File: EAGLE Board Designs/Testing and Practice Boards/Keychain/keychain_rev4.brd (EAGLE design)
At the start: 27.9 x 27.9 mm, 14 parts, among them J1 USB4110, U1 LM555

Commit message: DRC and cam file
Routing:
- net GND: track 4.91 -> 2.53 mm
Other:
- board text added: "Hytech Racing 2024"
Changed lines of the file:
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@@
 <vertex x="19.05" y="6.35"/>
 </polygon>
+<text x="27.051" y="0.762" size="0.6858" layer="22" rot="MR0">Hytech Racing 2024</text>
 </plain>
 <attributes>
@@
 </class>
 </classes>
-<designrules name="default">
-<description language="de">&lt;b&gt;EAGLE Design Rules&lt;/b&gt;
-&lt;p&gt;
-Die Standard-Design-Rules sind so gewählt, dass sie für
-die meisten Anwendungen passen. Sollte ihre Platine
-besondere Anforderungen haben, treffen Sie die erforderlichen
-Einstellungen hier und speichern die Design Rules unter
-einem neuen Namen ab.</description>
-<description language="en">&lt;b&gt;EAGLE Design Rules&lt;/b&gt;
+<designrules name="JLCPCB (2 Layer)">
+<description language="en">&lt;b&gt;JLCPCB Design Rules (2 Layers)&lt;/b&gt;
 &lt;p&gt;
 The default Design Rules have been set to cover
-a wide range of applications. Your particular design
-may have different requirements, so please make the
-necessary adjustments and save your customized
-design rules under a new name.</description>
+a wide range of applications.
+&lt;p&gt;
+Source: &lt;a href=&quot;https://jlcpcb.com/capabilities/Capabilities&quot;&gt;JLCPCB&lt;/a&gt;
+&lt;/p&gt;</description>
 <param name="layerSetup" value="(1*16)"/>
 <param name="mtCopper" value="0.035mm 0.035mm 0.035mm 0.035mm 0.035mm 0.035mm 0.035mm 0.035mm 0.035mm 0.035mm 0.035mm 0.035mm 0.035mm 0.035mm 0.035mm 0.035mm"/>
-<param name="mtIsolate" value="1.5mm 0.15mm 0.2mm 0.15mm 0.2mm 0.15mm 0.2mm 0.15mm 0.2mm 0.15mm 0.2mm 0.15mm 0.2mm 0.15mm 0.2mm"/>
-<param name="mdWireWire" value="6mil"/>
-<param name="mdWirePad" value="6mil"/>
-<param name="mdWireVia" value="6mil"/>
-<param name="mdPadPad" value="6mil"/>
-<param name="mdPadVia" value="6mil"/>
-<param name="mdViaVia" value="6mil"/>
-<param name="mdSmdPad" value="6mil"/>
-<param name="mdSmdVia" value="6mil"/>
-<param name="mdSmdSmd" value="6mil"/>
+<param name="mtIsolate" value="1.53mm 0.15mm 0.2mm 0.15mm 0.2mm 0.15mm 0.2mm 0.15mm 0.2mm 0.15mm 0.2mm 0.15mm 0.2mm 0.15mm 0.2mm"/>
+<param name="mdWireWire" value="5mil"/>
+<param name="mdWirePad" value="5mil"/>
+<param name="mdWireVia" value="8mil"/>
+<param name="mdPadPad" value="5mil"/>
+<param name="mdPadVia" value="10mil"/>
+<param name="mdViaVia" value="20mil"/>
+<param name="mdSmdPad" value="5mil"/>
+<param name="mdSmdVia" value="10mil"/>
+<param name="mdSmdSmd" value="5mil"/>
 <param name="mdViaViaSameLayer" value="6mil"/>
 <param name="mnLayersViaInSmd" value="2"/>
-<param name="mdCopperDimension" value="40mil"/>
-<param name="mdDrill" value="6mil"/>
+<param name="mdCopperDimension" value="0.2mm"/>
+<param name="mdDrill" value="21mil"/>
 <param name="mdSmdStop" value="0mil"/>
-<param name="msWidth" value="6mil"/>
-<param name="msDrill" value="0.35mm"/>
+<param name="msWidth" value="5mil"/>
+<param name="msDrill" value="0.3mm"/>
 <param name="msMicroVia" value="9.99mm"/>
 <param name="msBlindViaRatio" value="0.5"/>
@@
 <param name="rvViaOuter" value="0.25"/>
 <param name="rvViaInner" value="0.25"/>
-<param name="rvMicroViaOuter" value="0.25"/>
-<param name="rvMicroViaInner" value="0.25"/>
-<param name="rlMinPadTop" value="10mil"/>
+<param name="rvMicroViaOuter" value="0"/>
+<param name="rvMicroViaInner" value="0"/>
+<param name="rlMinPadTop" value="6mil"/>
 <param name="rlMaxPadTop" value="20mil"/>
-<param name="rlMinPadInner" value="10mil"/>
+<param name="rlMinPadInner" value="6mil"/>
 <param name="rlMaxPadInner" value="20mil"/>
-<param name="rlMinPadBottom" value="10mil"/>
+<param name="rlMinPadBottom" value="6mil"/>
 <param name="rlMaxPadBottom" value="20mil"/>
-<param name="rlMinViaOuter" value="8mil"/>
-<param name="rlMaxViaOuter" value="20mil"/>
-<param name="rlMinViaInner" value="8mil"/>
-<param name="rlMaxViaInner" value="20mil"/>
-<param name="rlMinMicroViaOuter" value="4mil"/>
+<param name="rlMinViaOuter" value="6mil"/>
+<param name="rlMaxViaOuter" value="12mil"/>
+<param name="rlMinViaInner" value="6mil"/>
+<param name="rlMaxViaInner" value="12mil"/>
+<param name="rlMinMicroViaOuter" value="6mil"/>
 <param name="rlMaxMicroViaOuter" value="20mil"/>
-<param name="rlMinMicroViaInner" value="4mil"/>
+<param name="rlMinMicroViaInner" value="6mil"/>
 <param name="rlMaxMicroViaInner" value="20mil"/>
 <param name="psTop" value="-1"/>
 <param name="psBottom" value="-1"/>
-<param name="psFirst" value="-1"/>
+<param name="psFirst" value="0"/>
 <param name="psElongationLong" value="100"/>
 <param name="psElongationOffset" value="100"/>
 <param name="mvStopFrame" value="1"/>
 <param name="mvCreamFrame" value="0"/>
-<param name="mlMinStopFrame" value="4mil"/>
-<param name="mlMaxStopFrame" value="4mil"/>
+<param name="mlMinStopFrame" value="6mil"/>
+<param name="mlMaxStopFrame" value="6mil"/>
 <param name="mlMinCreamFrame" value="0mil"/>
 <param name="mlMaxCreamFrame" value="0mil"/>
-<param name="mlViaStopLimit" value="0mil"/>
+<param name="mlViaStopLimit" value="30mil"/>
 <param name="srRoundness" value="0"/>
 <param name="srMinRoundness" value="0mil"/>
@@
 <param name="dpMaxLengthDifference" value="10mm"/>
 <param name="dpGapFactor" value="2.5"/>
-<param name="checkAngle" value="0"/>
+<param name="checkAngle" value="1"/>
 <param name="checkFont" value="1"/>
 <param name="checkRestrict" value="1"/>
 <param name="checkStop" value="0"/>
-<param name="checkValues" value="0"/>
+<param name="checkValues" value="1"/>
 <param name="checkNames" value="1"/>
 <param name="checkWireStubs" value="1"/>
-<param name="checkPolygonWidth" value="0"/>
+<param name="checkPolygonWidth" value="1"/>
 <param name="useDiameter" value="13"/>
-<param name="maxErrors" value="50"/>
+<param name="maxErrors" value="500"/>
 </designrules>
 <autorouter>
@@
 <attribute name="MOPN" value="667-ERJ-PB3B4122V" x="-5.334" y="39.624" size="1.778" layer="28" rot="MR90" display="off"/>
 <attribute name="MPN" value=" ERJ-PB3B4122V" x="-5.334" y="39.624" size="1.778" layer="28" rot="MR90" display="off"/>
-<attribute name="NAME" x="10.795" y="12.954" size="0.8128" layer="26" font="vector" rot="MR90" align="bottom-center"/>
+<attribute name="NAME" x="13.081" y="12.954" size="0.8128" layer="26" font="vector" rot="MR90" align="bottom-center"/>
 <attribute name="POWER" value="0.2W" x="-5.334" y="39.624" size="1.778" layer="28" rot="MR90" display="off"/>
 <attribute name="RESISTANCE" value="41.2k" x="-5.334" y="39.624" size="1.778" layer="28" rot="MR90" display="off"/>
@@
 <contactref element="J1" pad="S$1"/>
 <contactref element="J1" pad="S$2"/>
-<wire x1="8.8115" y1="20.7795" x2="8.0466" y2="20.0146" width="0.1524" layer="16"/>
-<wire x1="8.1915" y1="10.287" x2="8.3185" y2="10.414" width="0.1524" layer="16"/>
-<wire x1="10.033" y1="11.545" x2="9.889425" y2="11.401425" width="0.1524" layer="16"/>
-<wire x1="10.77" y1="20.228" x2="10.643" y2="20.101" width="0.1524" layer="16"/>
-<wire x1="9.363" y1="20.101" x2="9.144" y2="20.32" width="0.1524" layer="16"/>
-<wire x1="17.332" y1="20.066" x2="17.17" y2="20.228" width="0.1524" layer="16"/>
-<wire x1="18.022" y1="18.542" x2="18.022" y2="18.669" width="0.1524" layer="16"/>
 <polygon width="0.1524" layer="16">
 <vertex x="-0.381" y="-0.381"/>
@@
 <vertex x="-0.127" y="28.067"/>
 </polygon>
-<wire x1="8.86" y1="20.828" x2="8.8115" y2="20.7795" width="0.1524" layer="16"/>
-<via x="8.8115" y="20.7795" extent="1-16" drill="0.35"/>
 <wire x1="10.033" y1="11.545" x2="10.033" y2="11.799" width="0.1524" layer="16"/>
 <wire x1="10.033" y1="11.799" x2="9.132" y2="12.7" width="0.1524" layer="16"/>
 <wire x1="9.132" y1="12.7" x2="8.128" y2="12.7" width="0.1524" layer="16"/>
 <via x="8.128" y="12.7" extent="1-16" drill="0.35"/>
-<wire x1="8.86" y1="20.828" x2="9.144" y2="20.32" width="0" layer="19" extent="16-16"/>
+<via x="8.86" y="20.828" extent="1-16" drill="0.35"/>
 </signal>
 <signal name="+5V">
@@
 </signals>
 <mfgpreviewcolors>
-<mfgpreviewcolor name="soldermaskcolor" color="0xC8008000"/>
-<mfgpreviewcolor name="silkscreencolor" color="0xFFFEFEFE"/>
-<mfgpreviewcolor name="backgroundcolor" color="0xFF282828"/>
-<mfgpreviewcolor name="coppercolor" color="0xFFFFBF00"/>
+<mfgpreviewcolor name="soldermaskcolor" color="0xC8FFFFFF"/>
+<mfgpreviewcolor name="silkscreencolor" color="0xFF000000"/>
+<mfgpreviewcolor name="backgroundcolor" color="0xFF000000"/>
+<mfgpreviewcolor name="coppercolor" color="0xFFFFBB00"/>
 <mfgpreviewcolor name="substratecolor" color="0xFF786E46"/>
 </mfgpreviewcolors>

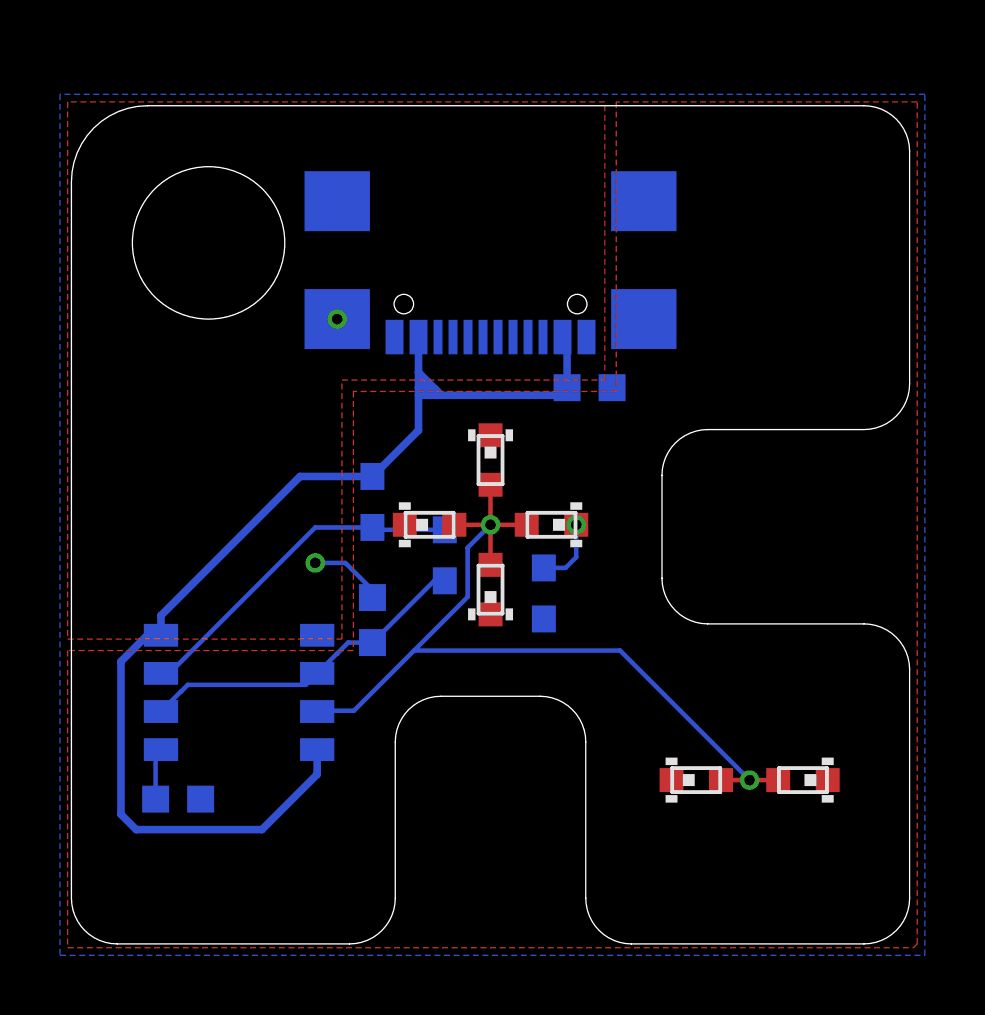
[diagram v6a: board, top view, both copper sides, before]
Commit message: Added resistors to CC1 and CC2 for actual functionality
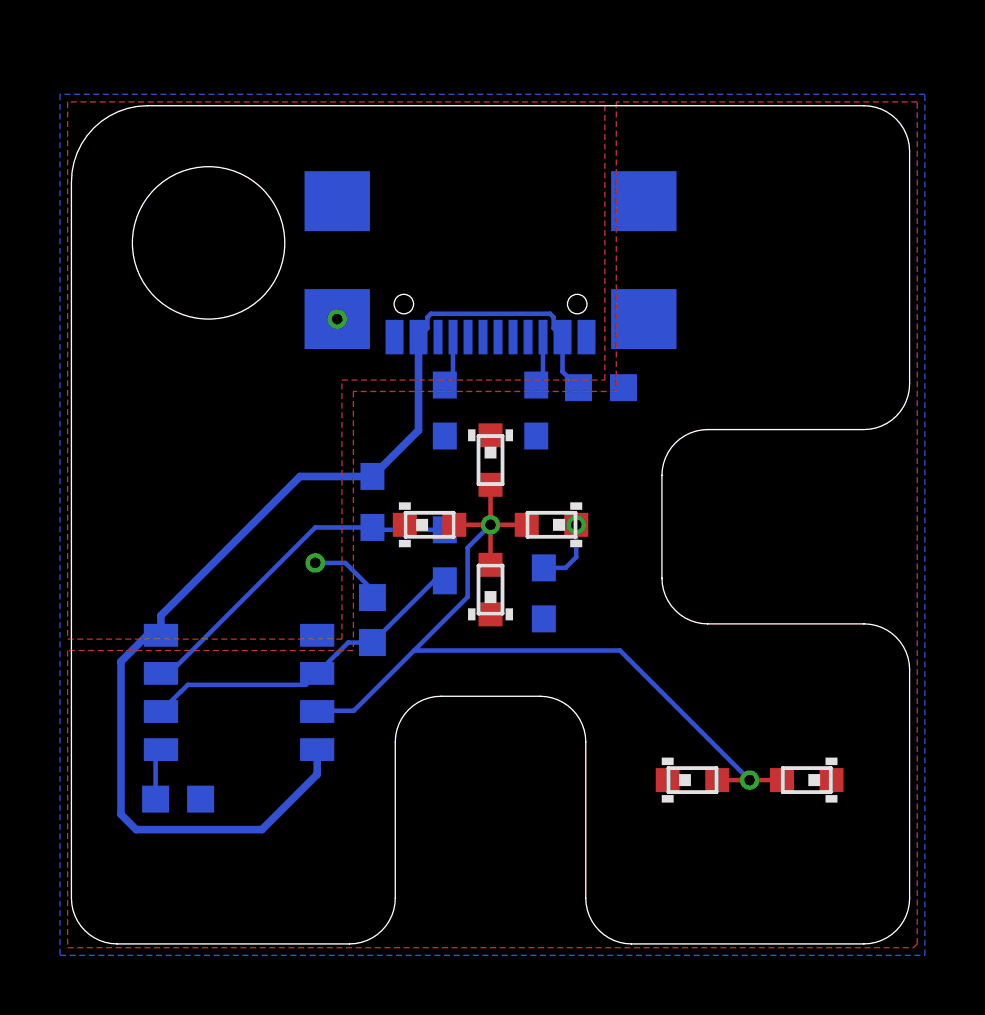
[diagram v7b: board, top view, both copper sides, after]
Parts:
- added R4, R5: RESISTOR_0603_5.1K, HyTechDevices:0603-RES
- moved C3 0.38 mm to (17.7, 18.5)
- moved D5 0.13 mm to (24.5, 5.46)
- moved D6 0.13 mm to (20.7, 5.46)
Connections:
- new net N$4: J1.P$4, R4.2
- new net N$5: J1.P$10, R5.2
- net GND: now also R4.1, R5.1
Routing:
- net +5V: track 39.8 -> 37.8 mm
- net N$4: track 0.00 -> 1.71 mm
- net N$5: track 0.00 -> 1.69 mm
